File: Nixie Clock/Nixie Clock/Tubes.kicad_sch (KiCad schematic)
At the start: 20 parts

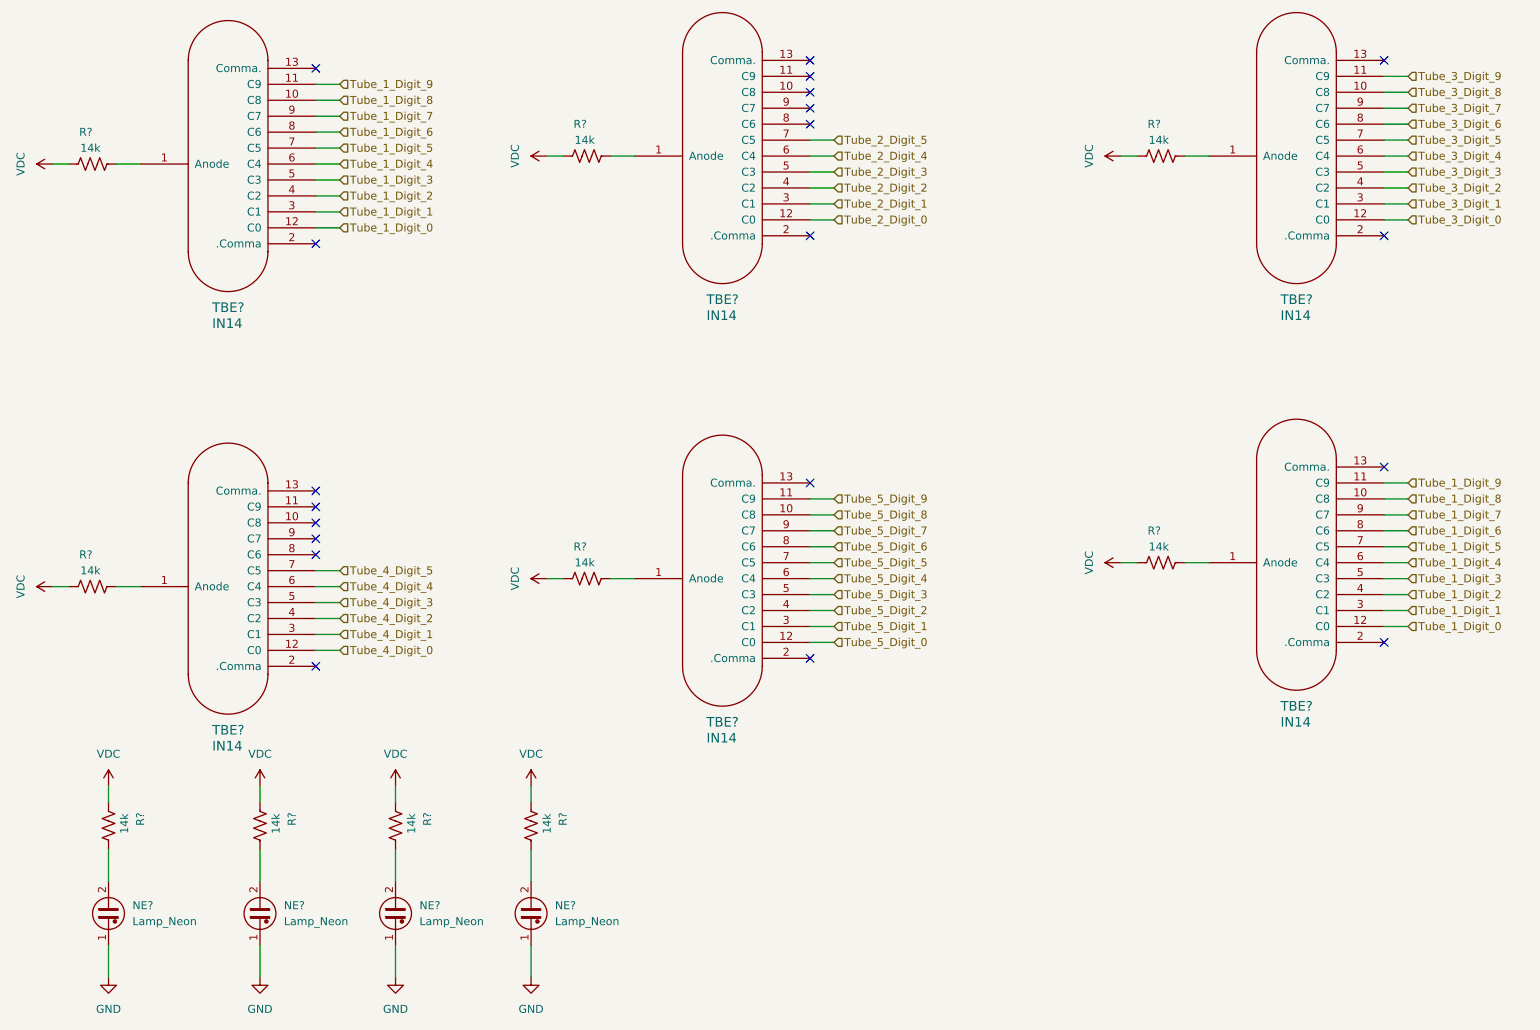
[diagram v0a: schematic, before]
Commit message: Need to add footprints for passives
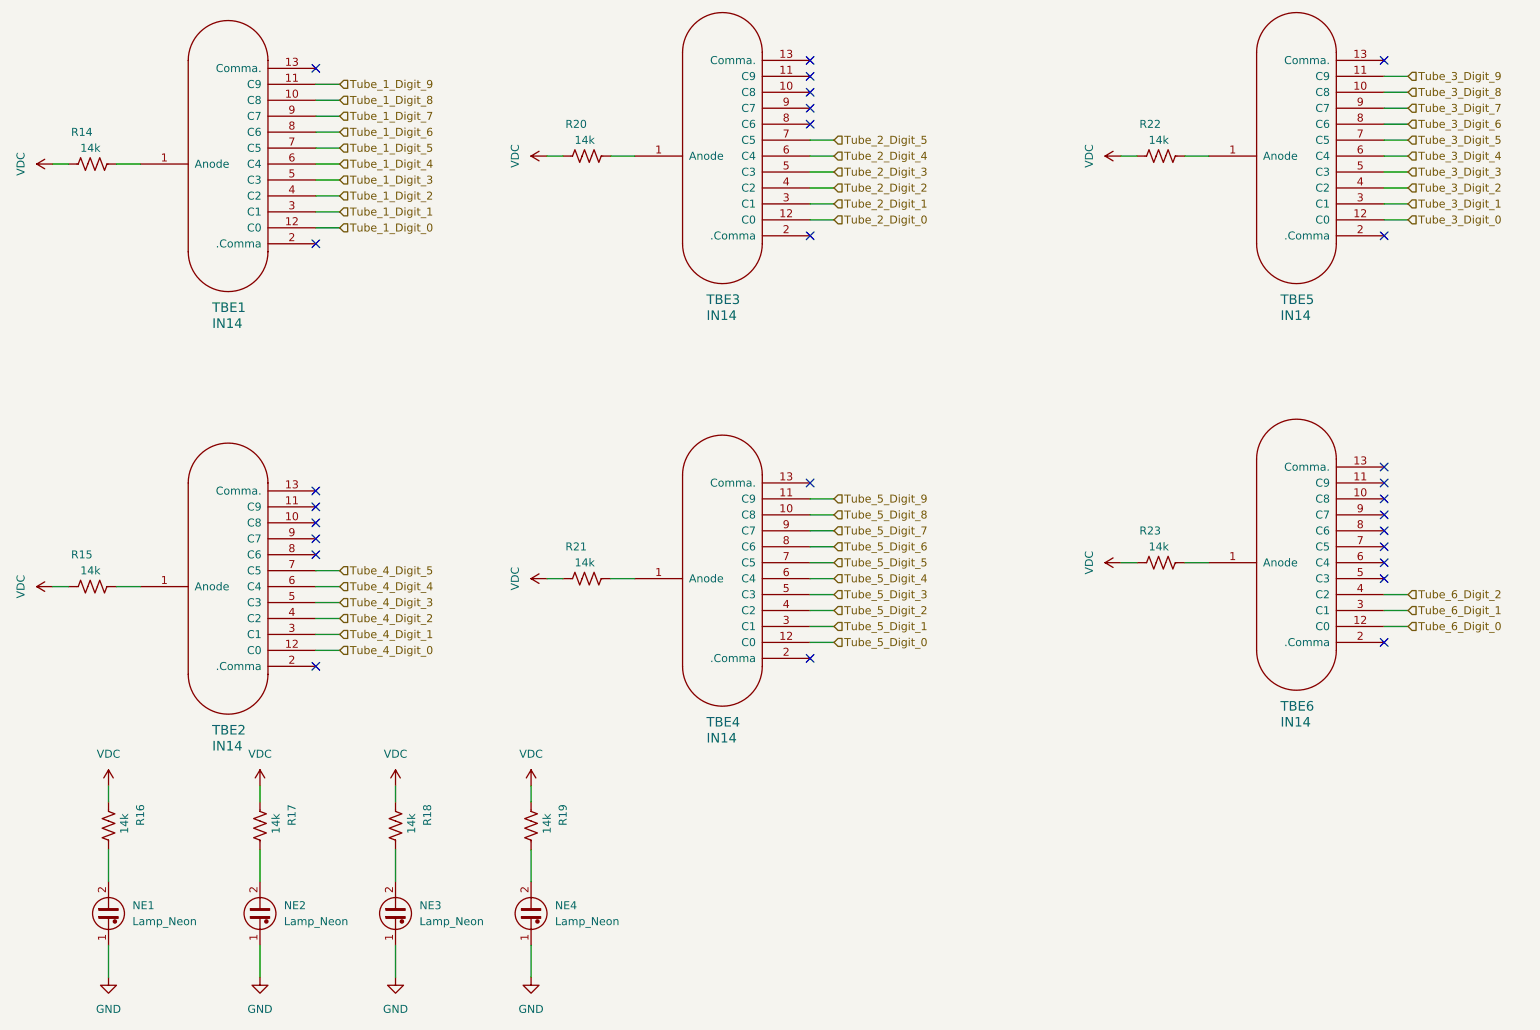
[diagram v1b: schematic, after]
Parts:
- removed NE? (x3): Lamp_Neon, symbol Device:Lamp_Neon
- added NE2, NE3, NE4: Lamp_Neon, LED_THT:LED_D5.0mm_Clear, symbol Device:Lamp_Neon
- NE1: renamed from NE?; footprint (none) -> LED_THT:LED_D5.0mm_Clear
- gave numbers to parts that had none: 16
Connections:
- net GND: now also NE2.1, NE3.1, NE4.1
- net Tube_1_Digit_0: no longer TBE6.12 (C0)
- net Tube_1_Digit_1: no longer TBE6.3 (C1)
- net Tube_1_Digit_2: no longer TBE6.4 (C2)
- net Tube_1_Digit_3: no longer TBE6.5 (C3)
- net Tube_1_Digit_4: no longer TBE6.6 (C4)
- net Tube_1_Digit_5: no longer TBE6.7 (C5)
- net Tube_1_Digit_6: no longer TBE6.8 (C6)
- net Tube_1_Digit_7: no longer TBE6.9 (C7)
- net Tube_1_Digit_8: no longer TBE6.10 (C8)
- net Tube_1_Digit_9: no longer TBE6.11 (C9)
- net at R17.1: now also NE2.2
- net at R18.1: now also NE3.2
- net at R19.1: now also NE4.2
- new net Tube_6_Digit_0: TBE6.12 (C0)
- new net Tube_6_Digit_1: TBE6.3 (C1)
- new net Tube_6_Digit_2: TBE6.4 (C2)
- no-connect marks 20 -> 27

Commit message: Started Routing
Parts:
- removed NE3, NE4: Lamp_Neon, LED_THT:LED_D5.0mm_Clear, symbol Device:Lamp_Neon
- removed R18, R19: 14k, symbol Device:R_US
- R14, R15, R16, R17, R20, R21, R22, R23: footprint (none) -> Resistor_THT:R_Axial_DIN0207_L6.3mm_D2.5mm_P10.16mm_Horizontal
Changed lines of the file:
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@@
-    (stroke (width 0) (type default) (color 0 0 0 0))
-  )
-  (wire (pts (xy 83.82 153.67) (xy 83.82 156.21))
     (stroke (width 0) (type default) (color 0 0 0 0))
   )
@@
     (stroke (width 0) (type default) (color 0 0 0 0))
   )
-  (wire (pts (xy 105.41 163.83) (xy 105.41 168.91))
-    (stroke (width 0) (type default) (color 0 0 0 0))
-  )
   (wire (pts (xy 39.37 54.61) (xy 43.18 54.61))
     (stroke (width 0) (type default) (color 0 0 0 0))
   )
-  (wire (pts (xy 83.82 179.07) (xy 83.82 184.15))
-    (stroke (width 0) (type default) (color 0 0 0 0))
-  )
   (wire (pts (xy 71.12 132.08) (xy 74.93 132.08))
     (stroke (width 0) (type default) (color 0 0 0 0))
@@
     (stroke (width 0) (type default) (color 0 0 0 0))
   )
-  (wire (pts (xy 105.41 153.67) (xy 105.41 156.21))
-    (stroke (width 0) (type default) (color 0 0 0 0))
-  )
   (wire (pts (xy 209.55 53.34) (xy 213.36 53.34))
     (stroke (width 0) (type default) (color 0 0 0 0))
@@
     (stroke (width 0) (type default) (color 0 0 0 0))
   )
-  (wire (pts (xy 83.82 163.83) (xy 83.82 168.91))
-    (stroke (width 0) (type default) (color 0 0 0 0))
-  )
   (wire (pts (xy 29.21 54.61) (xy 31.75 54.61))
     (stroke (width 0) (type default) (color 0 0 0 0))
@@
   )
   (wire (pts (xy 71.12 41.91) (xy 74.93 41.91))
-    (stroke (width 0) (type default) (color 0 0 0 0))
-  )
-  (wire (pts (xy 105.41 179.07) (xy 105.41 184.15))
     (stroke (width 0) (type default) (color 0 0 0 0))
   )
@@
     )
     (property "Datasheet" "" (id 3) (at 29.21 54.61 0)
-      (effects (font (size 1.27 1.27)) hide)
-    )
-    (pin "1")
-  )
-  (symbol (lib_id "power:GND") (at 83.82 184.15 0) (unit 1)
-    (in_bom yes) (on_board yes) (fields_autoplaced)
-    (property "Reference" "#PWR074" (id 0) (at 83.82 190.5 0)
-      (effects (font (size 1.27 1.27)) hide)
-    )
-    (property "Value" "GND" (id 1) (at 83.82 189.23 0))
-    (property "Footprint" "" (id 2) (at 83.82 184.15 0)
-      (effects (font (size 1.27 1.27)) hide)
-    )
-    (property "Datasheet" "" (id 3) (at 83.82 184.15 0)
       (effects (font (size 1.27 1.27)) hide)
     )
@@
       (effects (font (size 1.27 1.27)) (justify right))
     )
-    (property "Footprint" "" (id 2) (at 35.306 55.626 90)
+    (property "Footprint" "Resistor_THT:R_Axial_DIN0207_L6.3mm_D2.5mm_P10.16mm_Horizontal" (id 2) (at 35.306 55.626 90)
       (effects (font (size 1.27 1.27)) hide)
     )
@@
       (effects (font (size 1.27 1.27)) (justify right))
     )
-    (property "Footprint" "" (id 2) (at 61.214 159.766 90)
+    (property "Footprint" "Resistor_THT:R_Axial_DIN0207_L6.3mm_D2.5mm_P10.16mm_Horizontal" (id 2) (at 61.214 159.766 90)
       (effects (font (size 1.27 1.27)) hide)
     )
@@
     (pin "1")
   )
-  (symbol (lib_id "power:VDC") (at 83.82 153.67 0) (unit 1)
-    (in_bom yes) (on_board yes) (fields_autoplaced)
-    (property "Reference" "#PWR073" (id 0) (at 83.82 156.21 0)
-      (effects (font (size 1.27 1.27)) hide)
-    )
-    (property "Value" "VDC" (id 1) (at 83.82 148.59 0))
-    (property "Footprint" "" (id 2) (at 83.82 153.67 0)
-      (effects (font (size 1.27 1.27)) hide)
-    )
-    (property "Datasheet" "" (id 3) (at 83.82 153.67 0)
-      (effects (font (size 1.27 1.27)) hide)
-    )
-    (pin "1")
-  )
-  (symbol (lib_id "Device:Lamp_Neon") (at 105.41 173.99 0) (unit 1)
-    (in_bom yes) (on_board yes) (fields_autoplaced)
-    (property "Reference" "NE4" (id 0) (at 109.22 172.7199 0)
-      (effects (font (size 1.27 1.27)) (justify left))
-    )
-    (property "Value" "Lamp_Neon" (id 1) (at 109.22 175.2599 0)
-      (effects (font (size 1.27 1.27)) (justify left))
-    )
-    (property "Footprint" "LED_THT:LED_D5.0mm_Clear" (id 2) (at 105.41 171.45 90)
-      (effects (font (size 1.27 1.27)) hide)
-    )
-    (property "Datasheet" "~" (id 3) (at 105.41 171.45 90)
-      (effects (font (size 1.27 1.27)) hide)
-    )
-    (pin "1")
-    (pin "2")
-  )
-  (symbol (lib_id "power:GND") (at 105.41 184.15 0) (unit 1)
-    (in_bom yes) (on_board yes) (fields_autoplaced)
-    (property "Reference" "#PWR076" (id 0) (at 105.41 190.5 0)
-      (effects (font (size 1.27 1.27)) hide)
-    )
-    (property "Value" "GND" (id 1) (at 105.41 189.23 0))
-    (property "Footprint" "" (id 2) (at 105.41 184.15 0)
-      (effects (font (size 1.27 1.27)) hide)
-    )
-    (property "Datasheet" "" (id 3) (at 105.41 184.15 0)
-      (effects (font (size 1.27 1.27)) hide)
-    )
-    (pin "1")
-  )
   (symbol (lib_id "power:GND") (at 62.23 184.15 0) (unit 1)
     (in_bom yes) (on_board yes) (fields_autoplaced)
@@
       (effects (font (size 1.27 1.27)) (justify right))
     )
-    (property "Footprint" "" (id 2) (at 205.486 54.356 90)
+    (property "Footprint" "Resistor_THT:R_Axial_DIN0207_L6.3mm_D2.5mm_P10.16mm_Horizontal" (id 2) (at 205.486 54.356 90)
       (effects (font (size 1.27 1.27)) hide)
     )
@@
       (effects (font (size 1.27 1.27)) (justify right))
     )
-    (property "Footprint" "" (id 2) (at 37.084 159.766 90)
+    (property "Footprint" "Resistor_THT:R_Axial_DIN0207_L6.3mm_D2.5mm_P10.16mm_Horizontal" (id 2) (at 37.084 159.766 90)
       (effects (font (size 1.27 1.27)) hide)
     )
@@
       (effects (font (size 1.27 1.27)) (justify right))
     )
-    (property "Footprint" "" (id 2) (at 114.046 121.666 90)
+    (property "Footprint" "Resistor_THT:R_Axial_DIN0207_L6.3mm_D2.5mm_P10.16mm_Horizontal" (id 2) (at 114.046 121.666 90)
       (effects (font (size 1.27 1.27)) hide)
     )
     (property "Datasheet" "~" (id 3) (at 114.3 120.65 0)
-      (effects (font (size 1.27 1.27)) hide)
-    )
-    (pin "1")
-    (pin "2")
-  )
-  (symbol (lib_id "Device:R_US") (at 105.41 160.02 180) (unit 1)
-    (in_bom yes) (on_board yes)
-    (property "Reference" "R19" (id 0) (at 110.49 160.02 90)
-      (effects (font (size 1.27 1.27)) (justify right))
-    )
-    (property "Value" "14k" (id 1) (at 107.95 161.2899 90)
-      (effects (font (size 1.27 1.27)) (justify right))
-    )
-    (property "Footprint" "" (id 2) (at 104.394 159.766 90)
-      (effects (font (size 1.27 1.27)) hide)
-    )
-    (property "Datasheet" "~" (id 3) (at 105.41 160.02 0)
-      (effects (font (size 1.27 1.27)) hide)
-    )
-    (pin "1")
-    (pin "2")
-  )
-  (symbol (lib_id "Device:R_US") (at 83.82 160.02 180) (unit 1)
-    (in_bom yes) (on_board yes)
-    (property "Reference" "R18" (id 0) (at 88.9 160.02 90)
-      (effects (font (size 1.27 1.27)) (justify right))
-    )
-    (property "Value" "14k" (id 1) (at 86.36 161.2899 90)
-      (effects (font (size 1.27 1.27)) (justify right))
-    )
-    (property "Footprint" "" (id 2) (at 82.804 159.766 90)
-      (effects (font (size 1.27 1.27)) hide)
-    )
-    (property "Datasheet" "~" (id 3) (at 83.82 160.02 0)
       (effects (font (size 1.27 1.27)) hide)
     )
@@
     )
     (pin "1")
-  )
-  (symbol (lib_id "Device:Lamp_Neon") (at 83.82 173.99 0) (unit 1)
-    (in_bom yes) (on_board yes) (fields_autoplaced)
-    (property "Reference" "NE3" (id 0) (at 87.63 172.7199 0)
-      (effects (font (size 1.27 1.27)) (justify left))
-    )
-    (property "Value" "Lamp_Neon" (id 1) (at 87.63 175.2599 0)
-      (effects (font (size 1.27 1.27)) (justify left))
-    )
-    (property "Footprint" "LED_THT:LED_D5.0mm_Clear" (id 2) (at 83.82 171.45 90)
-      (effects (font (size 1.27 1.27)) hide)
-    )
-    (property "Datasheet" "~" (id 3) (at 83.82 171.45 90)
-      (effects (font (size 1.27 1.27)) hide)
-    )
-    (pin "1")
-    (pin "2")
   )
   (symbol (lib_id "in14_lib:IN14") (at 49.53 129.54 90) (unit 1)
@@
       (effects (font (size 1.27 1.27)) (justify right))
     )
-    (property "Footprint" "" (id 2) (at 114.046 54.356 90)
+    (property "Footprint" "Resistor_THT:R_Axial_DIN0207_L6.3mm_D2.5mm_P10.16mm_Horizontal" (id 2) (at 114.046 54.356 90)
       (effects (font (size 1.27 1.27)) hide)
     )
@@
     (pin "1")
     (pin "2")
-  )
-  (symbol (lib_id "power:VDC") (at 105.41 153.67 0) (unit 1)
-    (in_bom yes) (on_board yes) (fields_autoplaced)
-    (property "Reference" "#PWR075" (id 0) (at 105.41 156.21 0)
-      (effects (font (size 1.27 1.27)) hide)
-    )
-    (property "Value" "VDC" (id 1) (at 105.41 148.59 0))
-    (property "Footprint" "" (id 2) (at 105.41 153.67 0)
-      (effects (font (size 1.27 1.27)) hide)
-    )
-    (property "Datasheet" "" (id 3) (at 105.41 153.67 0)
-      (effects (font (size 1.27 1.27)) hide)
-    )
-    (pin "1")
   )
   (symbol (lib_id "Device:Lamp_Neon") (at 62.23 173.99 0) (unit 1)
@@
       (effects (font (size 1.27 1.27)) (justify right))
     )
-    (property "Footprint" "" (id 2) (at 35.306 122.936 90)
+    (property "Footprint" "Resistor_THT:R_Axial_DIN0207_L6.3mm_D2.5mm_P10.16mm_Horizontal" (id 2) (at 35.306 122.936 90)
       (effects (font (size 1.27 1.27)) hide)
     )
@@
       (effects (font (size 1.27 1.27)) (justify right))
     )
-    (property "Footprint" "" (id 2) (at 205.486 119.126 90)
-      (effects (font (size 1.27 1.27)) hide)
-    )
+    (property "Footprint" "Resistor_THT:R_Axial_DIN0207_L6.3mm_D2.5mm_P10.16mm_Horizontal" (id 2) (at 205.486 119.126 90)
+      (effects (font (size 1.27 1.27)) hide)
+    )
